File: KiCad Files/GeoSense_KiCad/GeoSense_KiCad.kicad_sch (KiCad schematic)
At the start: 106 parts, among them J1 Conn_01x08_Pin, J2 Conn_01x17_Pin, U1 LM324, U10 LM324, U11 LM334Z, U12 LM334Z, U13 LM334Z, U14 LM334Z, U15 LM334Z, U16 LM334Z, U17 LM324, U18 LM324, U19 LM324, U2 LM334Z, U20 LM324, U21 LM334Z, U22 LM334Z, U23 LM334Z, U24 LM334Z, U3 LM334Z, U4 LM334Z, U5 LM324, U6 LM334Z, U7 LM334Z, U8 LM334Z, U9 LM324

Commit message: added the jumpers
added the jumper connections to allow for transition between a 4 and 2 wire thermistor.
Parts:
- removed J2: Conn_01x17_Pin, symbol Connector:Conn_01x17_Pin
- added J3: Conn_01x34_Pin, symbol Connector:Conn_01x34_Pin
- added JP1, JP2, JP3, JP4, JP5, JP6, JP7, JP8: SolderJumper_2_Open, symbol Jumper:SolderJumper_2_Open
- renumbered U3 to U1.1, U4 to U1.2, U17 to U2, U13 to U2.1, U21 to U2.2, U5 to U3, U2 to U3.1, U6 to U3.2, U18 to U4, U14 to U4.1, U22 to U4.2, U9 to U5, U7 to U5.1, U11 to U5.2, U19 to U6, U15 to U6.1, U23 to U6.2, U10 to U7, U8 to U7.1, U12 to U7.2, U20 to U8, U16 to U8.1, U24 to U8.2
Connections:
- net +5V: now also J3.1 (Pin_1)
- net GND: now also J3.10 (Pin_10), J3.13 (Pin_13), J3.14 (Pin_14), J3.17 (Pin_17), J3.18 (Pin_18), J3.2 (Pin_2), J3.21 (Pin_21), J3.22 (Pin_22), J3.25 (Pin_25), J3.26 (Pin_26), J3.29 (Pin_29), J3.30 (Pin_30), J3.33 (Pin_33), J3.34 (Pin_34), J3.5 (Pin_5), J3.6 (Pin_6), J3.9 (Pin_9)
- net Out 1: now also R6.1, U1.8
- net Out 2: now also R77.1, U2.8
- net Out 3: now also R20.1, U3.8
- net Out 4: now also R78.1, U4.8
- net Out 5: now also R39.1, U5.8
- net Out 6: now also R79.1, U6.8
- net Out 7: now also R40.1, U7.8
- net Out 8: now also R80.1, U8.8
- net T2.1 In: now reaches R41.2, U2.1.3
- net T2.1 In: now also J3.7 (Pin_7), JP2.2 (B)
- net T3.C: now reaches U3.3 (+)
- net T3.C: now also R12.1, R13.2, U3.2.3
- net T1.C: now reaches R10.1, R9.2, U1.2.3
- net T1.C: now also U1.3 (+)
- net T1.1 In: now reaches R8.2, U1.1.3
- net T1.1 In: now also J3.3 (Pin_3), JP1.2 (B)
- net T2.2 In: now reaches U2.6 (-)
- net T2.2 In: now also J3.8 (Pin_8), JP2.1 (A)
- net T7.2 In: now reaches U7.6 (-)
- net T7.2 In: now also J3.28 (Pin_28), JP7.1 (A)
- net T4.C: now reaches R46.1, R50.2, U4.2.3
- net T4.C: now also U4.3 (+)
- net T8.1 In: now reaches R44.2, U8.1.3
- net T8.1 In: now also J3.31 (Pin_31), JP8.2 (B)
- net T6.C: now reaches R47.1, R51.2, U6.2.3
- net T6.C: now also U6.3 (+)
- net T5.2 In: now reaches U5.6 (-)
- net T5.2 In: now also J3.20 (Pin_20), JP5.1 (A)
- net T5.C: now reaches R23.1, R25.2, U5.2.3
- net T5.C: now also U5.3 (+)
- net T4.1 In: now reaches R42.2, U4.1.3
- net T4.1 In: now also J3.15 (Pin_15), JP4.2 (B)
- net T5.1 In: now reaches R21.2, U5.1.3
- net T5.1 In: now also J3.19 (Pin_19), JP5.2 (B)
- net T7.C: now reaches R24.1, R26.2, U7.2.3
- net T7.C: now also U7.3 (+)
- net T4.2 In: now reaches U4.6 (-)
- net T4.2 In: now also J3.16 (Pin_16), JP4.1 (A)
- net T8.2 In: now reaches U8.6 (-)
- net T8.2 In: now also J3.32 (Pin_32), JP8.1 (A)
- net T8.C: now reaches R48.1, R52.2, U8.2.3
- net T8.C: now also U8.3 (+)
- net T6.1 In: now reaches R43.2, U6.1.3
- net T6.1 In: now also J3.23 (Pin_23), JP6.2 (B)
- net T2.C: now reaches R45.1, R49.2, U2.2.3
- net T2.C: now also U2.3 (+)
- net T6.2 In: now reaches U6.6 (-)
- net T6.2 In: now also J3.24 (Pin_24), JP6.1 (A)
- net T7.1 In: now reaches R22.2, U7.1.3
- net T7.1 In: now also J3.27 (Pin_27), JP7.2 (B)
- net T1.3 In: now reaches R11.2, U3.1.3
- net T1.3 In: now also U3.6 (-), JP3.1 (A), JP3.2 (B)
- net T1.2 In: now reaches U1.6 (-)
- net T1.2 In: now also J3.4 (Pin_4), JP1.1 (A)
- new net T3.1 In: J3.11 (Pin_11)
- new net T3.2 In: J3.12 (Pin_12)
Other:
- note added: "Double the input pins for a quad wire configuartion. with a solder jumper/connecter to return the pin configuration to the protype board. (Done) Add a groung pin to connect to the power supply (Done)"
- note added: "Power"
- note added: "T1"
- note added: "T2"
- note added: "T3"
- note added: "T4"
- note added: "T5"
- note added: "T6"
- note added: "T7"
- note added: "T8"
- note removed: "Double the input pins for a quad wire configuartion. with a solder jumper/connecter to return the pin configuration to the protype board. Add a groung pin to connect to the power supply"
- moved on the sheet: R10, R8, R9, U1.1, U1.2

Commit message: 2/7/25
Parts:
- removed J3: Conn_01x34_Pin, symbol Connector:Conn_01x34_Pin
- added J1, J2, J3, J4, J5, J6, J7, J8: Conn_01x04_Pin, symbol Connector:Conn_01x04_Pin
- added JP: Conn_01x02_Pin, symbol Connector:Conn_01x02_Pin
- JP1, JP2, JP3, JP4, JP5, JP6, JP7, JP8: footprint (none) -> Jumper:SolderJumper-2_P1.3mm_Open_RoundedPad1.0x1.5mm
- renumbered J1 to JO
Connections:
- net +5V: now also JP.1 (Pin_1)
- net GND: now also J1.3 (Pin_3), J1.4 (Pin_4), J2.3 (Pin_3), J2.4 (Pin_4), J3.3 (Pin_3), J3.4 (Pin_4), J4.3 (Pin_3), J4.4 (Pin_4), J5.3 (Pin_3), J5.4 (Pin_4), J6.3 (Pin_3), J6.4 (Pin_4), J7.3 (Pin_3), J7.4 (Pin_4), J8.3 (Pin_3), J8.4 (Pin_4), JP.2 (Pin_2)
- net T1.1 In: now also J1.1 (Pin_1)
- net T1.2 In: now also J1.2 (Pin_2)
- net T2.1 In: now also J2.1 (Pin_1)
- net T2.2 In: now also J2.2 (Pin_2)
- net T3.1 In: now also J3.1 (Pin_1)
- net T3.2 In: now also J3.2 (Pin_2)
- net T4.1 In: now also J4.1 (Pin_1)
- net T4.2 In: now also J4.2 (Pin_2)
- net T5.1 In: now also J5.1 (Pin_1)
- net T5.2 In: now also J5.2 (Pin_2)
- net T6.1 In: now also J6.1 (Pin_1)
- net T6.2 In: now also J6.2 (Pin_2)
- net T7.1 In: now also J7.1 (Pin_1)
- net T7.2 In: now also J7.2 (Pin_2)
- net T8.1 In: now also J8.1 (Pin_1)
- net T8.2 In: now also J8.2 (Pin_2)
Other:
- note added: "Double the input pins for a quad wire configuartion. with a solder jumper/connecter to return the pin configuration to the protype board. (Done) Add a groung pin to connect to the power supply (Done) Split the in terminal block to sets of 4 for each module and a set of 2 for power. Add the screwhole junctions"
- note removed: "Double the input pins for a quad wire configuartion. with a solder jumper/connecter to return the pin configuration to the protype board. (Done) Add a groung pin to connect to the power supply (Done)"

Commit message: finished the schematic
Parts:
- removed JO: Conn_01x08_Pin, symbol Connector:Conn_01x08_Pin
- added J10, J11, J12, J13: Conn_01x01_Socket, MountingHole:MountingHole_3.2mm_M3_DIN965_Pad_TopBottom, symbol Connector:Conn_01x01_Socket
- added J9: Conn_01x08_Pin, Connector_PinHeader_2.54mm:PinHeader_1x08_P2.54mm_Horizontal, symbol Connector:Conn_01x08_Pin
- added unit 4 of U1
- added unit 4 of U2
- added unit 4 of U3
- added unit 4 of U4
- added unit 4 of U5
- added unit 4 of U6
- added unit 4 of U7
- added unit 4 of U8
- J0: renamed from JP; footprint (none) -> Connector_PinHeader_2.54mm:PinHeader_1x02_P2.54mm_Vertical
- J1, J2, J3, J4, J5, J6, J7, J8: footprint (none) -> Connector_PinHeader_2.54mm:PinHeader_1x04_P2.54mm_Horizontal
- R1, R10, R11, R12, R13, R14, R15, R16, R17, R18, R19, R2, R20, R21, R22, R23, R24, R25, R26, R27, R28, R29, R3, R30, R31, R32, R33, R34, R35, R36, R37, R38, R39, R4, R40, R41, R42, R43, R44, R45, R46, R47, R48, R49, R5, R50, R51, R52, R53, R54, R55, R56, R57, R58, R59, R6, R60, R61, R62, R63, R64, R65, R66, R67, R68, R69, R7, R70, R71, R72, R73, R74, R75, R76, R77, R78, R79, R8, R80, R9: footprint (none) -> Resistor_THT:R_Axial_DIN0204_L3.6mm_D1.6mm_P5.08mm_Horizontal
- renumbered U17 to U2, U5 to U3, U18 to U4, U9 to U5, U19 to U6, U10 to U7, U20 to U8
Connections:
- net GND: now also J10.1 (Pin_1), J11.1 (Pin_1), J12.1 (Pin_1), J13.1 (Pin_1)
- net Out 1: now also J9.1 (Pin_1)
- net Out 2: now also J9.2 (Pin_2)
- net Out 3: now also J9.3 (Pin_3)
- net Out 4: now also J9.4 (Pin_4)
- net Out 5: now also J9.5 (Pin_5)
- net Out 6: now also J9.6 (Pin_6)
- net Out 7: now also J9.7 (Pin_7)
- net Out 8: now also J9.8 (Pin_8)
- net T3.1 In: now also JP3.2 (B), R11.2, U3.1.3
- net T3.2 In: now also JP3.1 (A), U3.6 (-)
- removed net T1.3 In: JP3.1 (A), JP3.2 (B), R11.2, U3.1.3, U3.6 (-)
- no-connect marks 0 -> 24
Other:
- note removed: "Change Notes:"
- note removed: "Double the input pins for a quad wire configuartion. with a solder jumper/connecter to return the pin configuration to the protype board. (Done) Add a groung pin to connect to the power supply (Done) Split the in terminal block to sets of 4 for each module and a set of 2 for power. Add the screwhole junctions"
- moved on the sheet: J2, J3, J4, J5, J6, J7, J8, JP1, JP2, JP4, JP5, JP6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

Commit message: added logo
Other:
- title: GeoSense 8 modual sensing circuit -> GeoSense 8 module sensing circuit
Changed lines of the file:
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@@
 	(paper "A3")
 	(title_block
-		(title "GeoSense 8 modual sensing circuit")
+		(title "GeoSense 8 module sensing circuit")
 		(date "2025-01-14")
 		(rev "1")

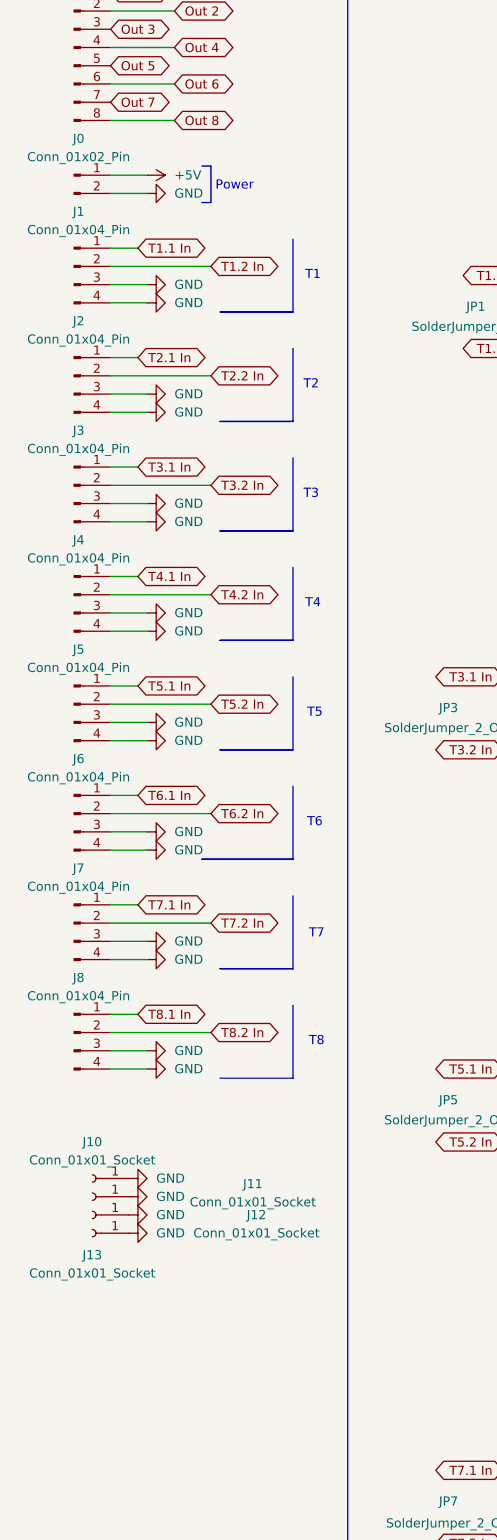
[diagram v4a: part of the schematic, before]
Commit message: fixed wrong 3rd stage opamp wiring
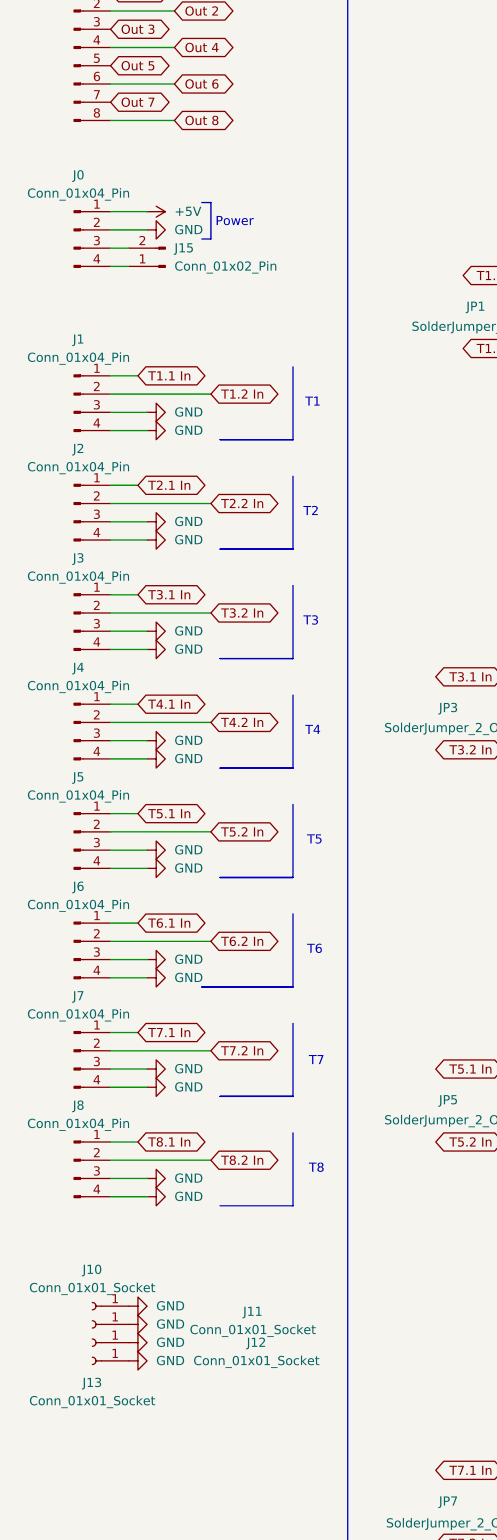
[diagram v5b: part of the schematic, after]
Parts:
- removed J0: Conn_01x02_Pin, Connector_PinHeader_2.54mm:PinHeader_1x02_P2.54mm_Vertical, symbol Connector:Conn_01x02_Pin
- added J0: Conn_01x04_Pin, Connector_PinHeader_2.54mm:PinHeader_1x04_P2.54mm_Horizontal, symbol Connector:Conn_01x04_Pin
- added J15: Conn_01x02_Pin, Connector_PinHeader_2.54mm:PinHeader_1x02_P2.54mm_Vertical, symbol Connector:Conn_01x02_Pin
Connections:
- net +5V: now also J0.1 (Pin_1)
- net GND: now also J0.2 (Pin_2)
- new net: J0.3 (Pin_3), J15.2 (Pin_2)
- new net: J0.4 (Pin_4), J15.1 (Pin_1)
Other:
- moved on the sheet: J1, J10, J11, J12, J13, J2, J3, J4, J5, J6, J7, J8

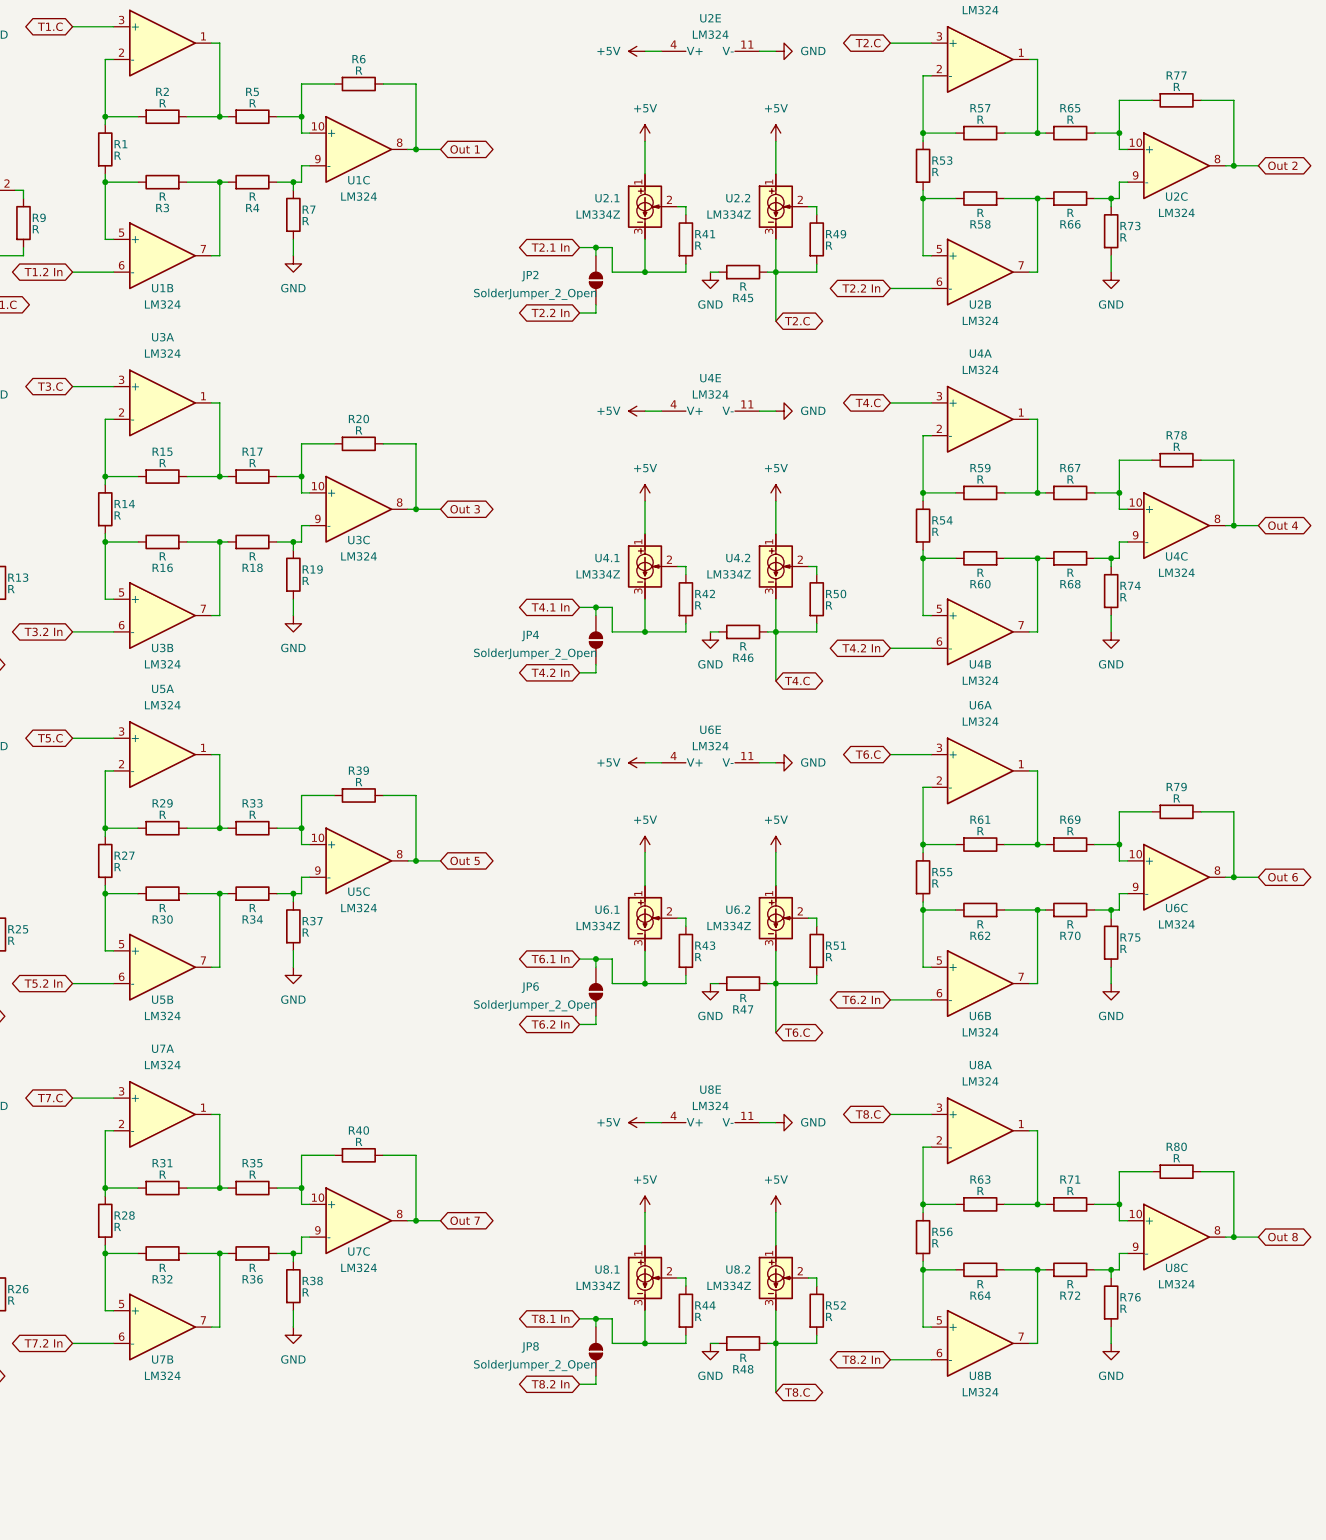
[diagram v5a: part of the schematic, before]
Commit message: fixed opamp conections
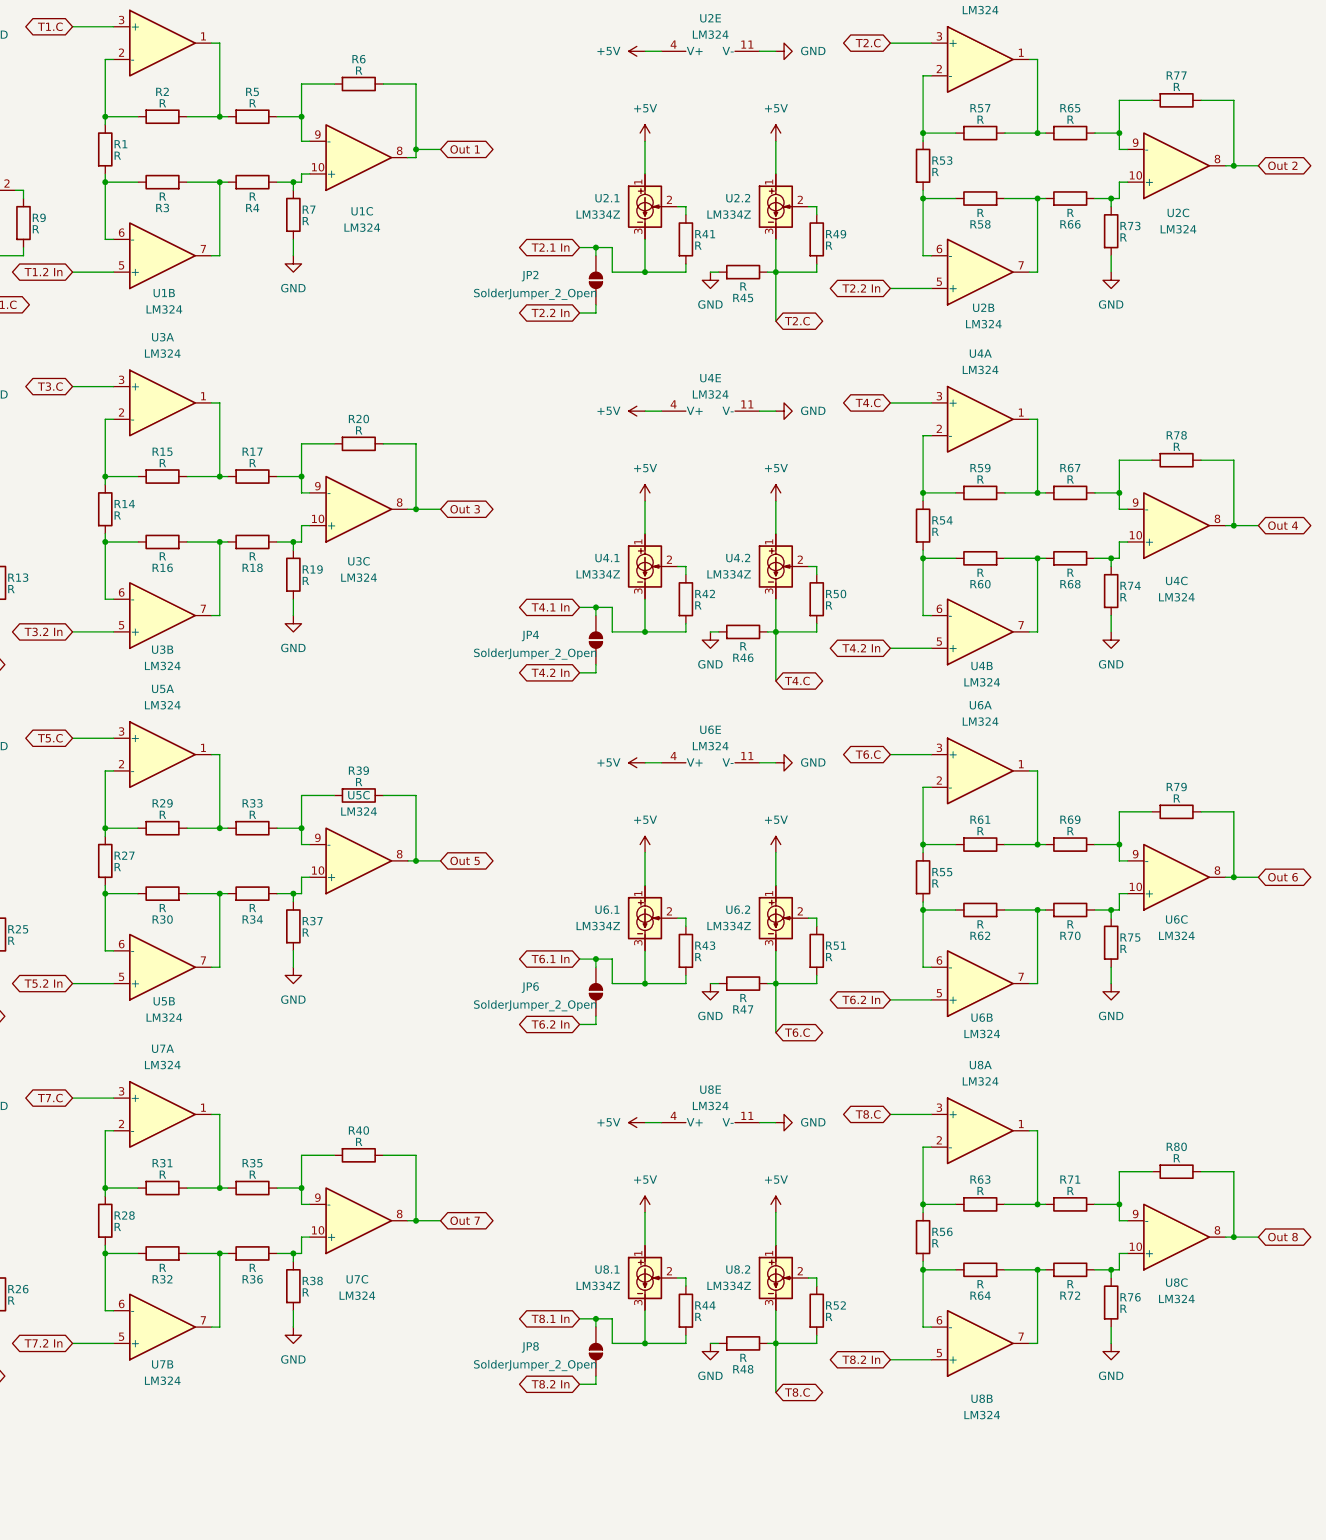
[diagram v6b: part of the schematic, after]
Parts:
- U1, U2, U3, U4, U5, U6, U7, U8: footprint Package_SO:TSSOP-14_4.4x5mm_P0.65mm -> (none)
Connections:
- net T1.2 In: now also U1.5 (+); no longer U1.6 (-)
- net T2.2 In: now also U2.5 (+); no longer U2.6 (-)
- net T3.2 In: now also U3.5 (+); no longer U3.6 (-)
- net T4.2 In: now also U4.5 (+); no longer U4.6 (-)
- net T5.2 In: now also U5.5 (+); no longer U5.6 (-)
- net T6.2 In: now also U6.5 (+); no longer U6.6 (-)
- net T7.2 In: now also U7.5 (+); no longer U7.6 (-)
- net T8.2 In: now also U8.5 (+); no longer U8.6 (-)
- net at R5.1, R6.2: now also U1.9 (-); no longer U1.10 (+)
- net at R4.1, R7.1: now also U1.10 (+); no longer U1.9 (-)
- net at R54.2, R60.1: now also U4.6 (-); no longer U4.5 (+)
- net at R55.2, R62.1: now also U6.6 (-); no longer U6.5 (+)
- net at R68.1, R74.1: now also U4.10 (+); no longer U4.9 (-)
- net at R66.1, R73.1: now also U2.10 (+); no longer U2.9 (-)
- net at R69.1, R79.2: now also U6.9 (-); no longer U6.10 (+)
- net at R70.1, R75.1: now also U6.10 (+); no longer U6.9 (-)
- net at R17.1, R20.2: now also U3.9 (-); no longer U3.10 (+)
- net at R35.1, R40.2: now also U7.9 (-); no longer U7.10 (+)
- net at R36.1, R38.1: now also U7.10 (+); no longer U7.9 (-)
- net at R65.1, R77.2: now also U2.9 (-); no longer U2.10 (+)
- net at R67.1, R78.2: now also U4.9 (-); no longer U4.10 (+)
- net at R27.2, R30.1: now also U5.6 (-); no longer U5.5 (+)
- net at R53.2, R58.1: now also U2.6 (-); no longer U2.5 (+)
- net at R18.1, R19.1: now also U3.10 (+); no longer U3.9 (-)
- net at R56.2, R64.1: now also U8.6 (-); no longer U8.5 (+)
- net at R28.2, R32.1: now also U7.6 (-); no longer U7.5 (+)
- net at R1.2, R3.1: now also U1.6 (-); no longer U1.5 (+)
- net at R72.1, R76.1: now also U8.10 (+); no longer U8.9 (-)
- net at R14.2, R16.1: now also U3.6 (-); no longer U3.5 (+)
- net at R33.1, R39.2: now also U5.9 (-); no longer U5.10 (+)
- net at R34.1, R37.1: now also U5.10 (+); no longer U5.9 (-)
- net at R71.1, R80.2: now also U8.9 (-); no longer U8.10 (+)
